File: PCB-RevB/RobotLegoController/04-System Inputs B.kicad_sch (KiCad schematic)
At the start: 119 parts, among them Q11 BSS84, Q12 BSS84

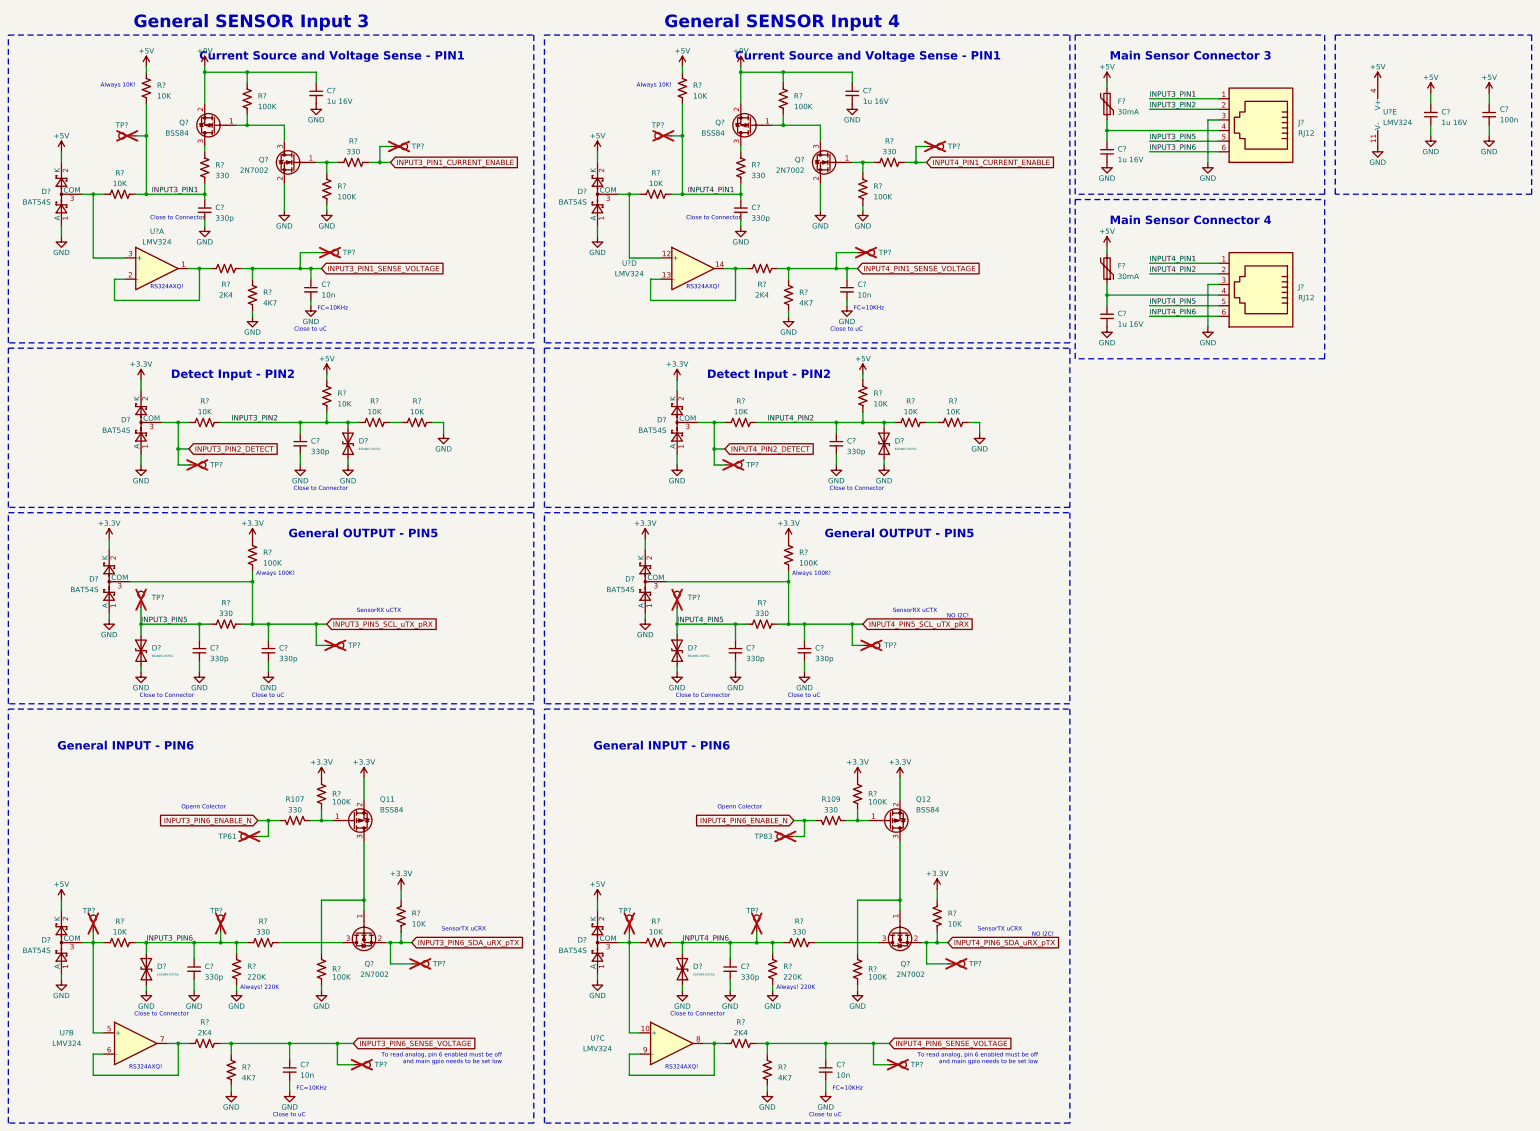
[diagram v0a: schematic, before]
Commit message: Finish updating schematic REV B
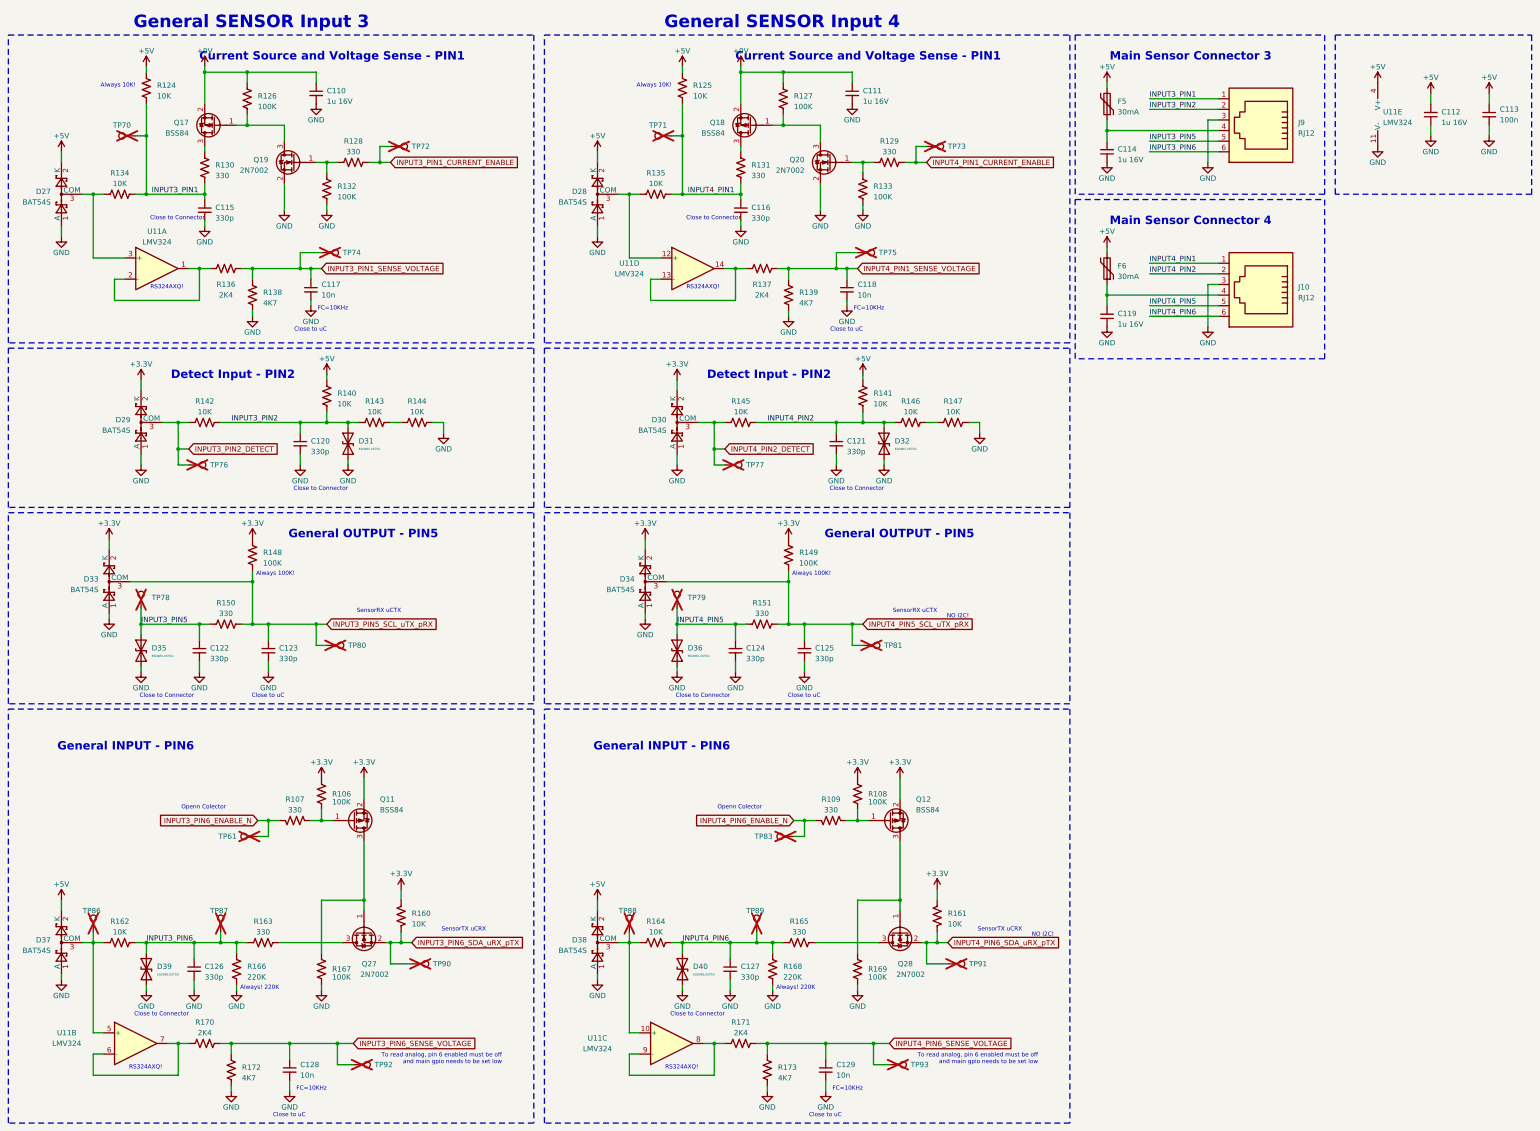
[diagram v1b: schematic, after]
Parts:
- J10, J9: renamed from J?; footprint Connector_RJ:RJ12_Amphenol_54601 -> Connector_RJ:RJ25_Wayconn_MJEA-660X1_Horizontal
- gave numbers to parts that had none: 107
